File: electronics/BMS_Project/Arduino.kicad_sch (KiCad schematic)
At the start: 1 part

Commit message: Meeting 28.04.2023 worked on schematic
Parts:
- added JP1: SolderJumper_2_Open, symbol Jumper:SolderJumper_2_Open
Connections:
- net +5V: now also JP1.1 (A)
- net at XA1.AREF: now also JP1.2 (B)
- net switch_for_disconnecting_batteries renamed bat_main_switch
- no-connect marks 65 -> 64
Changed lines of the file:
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@@
   (no_connect (at 148.59 55.88))
   (no_connect (at 148.59 104.14))
-  (no_connect (at 82.55 114.3))
   (no_connect (at 82.55 40.64))
   (no_connect (at 148.59 45.72))
@@
     (stroke (width 0) (type default))
   )
+  (wire (pts (xy 66.04 114.3) (xy 69.85 114.3))
+    (stroke (width 0) (type default))
+  )
   (wire (pts (xy 72.39 137.16) (xy 82.55 137.16))
     (stroke (width 0) (type default))
@@
   )
   (wire (pts (xy 82.55 149.86) (xy 82.55 153.67))
+    (stroke (width 0) (type default))
+  )
+  (wire (pts (xy 77.47 114.3) (xy 82.55 114.3))
     (stroke (width 0) (type default))
   )
@@
     (effects (font (size 1.27 1.27)) (justify left))
   )
-  (hierarchical_label "switch_for_disconnecting_batteries" (shape bidirectional) (at 148.59 81.28 0) (fields_autoplaced)
+  (hierarchical_label "bat_main_switch" (shape bidirectional) (at 148.59 81.28 0) (fields_autoplaced)
     (effects (font (size 1.27 1.27)) (justify left))
   )
@@
     (effects (font (size 1.27 1.27)) (justify left))
   )
+  (symbol (lib_id "Jumper:SolderJumper_2_Open") (at 73.66 114.3 0) (unit 1)
+    (in_bom yes) (on_board yes) (dnp no)
+    (property "Reference" "JP1" (at 72.39 111.76 0)
+      (effects (font (size 1.27 1.27)))
+    )
+    (property "Value" "SolderJumper_2_Open" (at 64.77 118.11 0)
+      (effects (font (size 1.27 1.27)))
+    )
+    (property "Footprint" "" (at 73.66 114.3 0)
+      (effects (font (size 1.27 1.27)) hide)
+    )
+    (property "Datasheet" "~" (at 73.66 114.3 0)
+      (effects (font (size 1.27 1.27)) hide)
+    )
+    (pin "1")
+    (pin "2")
+    (instances
+      (project "BMS_Project"
+        (path "/524e7f14-feb0-4ca2-9425-a347c869bfa6/991268b7-e362-463f-9f04-bcec0fe70615"
+          (reference "JP1") (unit 1)
+        )
+      )
+    )
+  )
+  (symbol (lib_id "power:+5V") (at 66.04 114.3 0) (unit 1)
+    (in_bom yes) (on_board yes) (dnp no) (fields_autoplaced)
+    (property "Reference" "#PWR013" (at 66.04 118.11 0)
+      (effects (font (size 1.27 1.27)) hide)
+    )
+    (property "Value" "+5V" (at 66.04 110.49 0)
+      (effects (font (size 1.27 1.27)))
+    )
+    (property "Footprint" "" (at 66.04 114.3 0)
+      (effects (font (size 1.27 1.27)) hide)
+    )
+    (property "Datasheet" "" (at 66.04 114.3 0)
+      (effects (font (size 1.27 1.27)) hide)
+    )
+    (pin "1")
+    (instances
+      (project "BMS_Project"
+        (path "/524e7f14-feb0-4ca2-9425-a347c869bfa6/991268b7-e362-463f-9f04-bcec0fe70615"
+          (reference "#PWR013") (unit 1)
+        )
+      )
+    )
+  )
   (symbol (lib_id "power:+3.3V") (at 72.39 137.16 0) (unit 1)

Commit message: discord session with Johannes and Fabian, Schematic nearly done, all footprints fields filled
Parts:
- added SW1, SW3, SW4, SW5: SW_Push, Button_Switch_SMD:SW_Push_1P1T_NO_6x6mm_H9.5mm, symbol Switch:SW_Push
- JP1: footprint (none) -> Jumper:SolderJumper-2_P1.3mm_Open_Pad1.0x1.5mm
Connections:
- net +5V: now also SW1.2, SW3.2, SW4.2, SW5.2
- net Switch_0: now reaches XA1.D30
- net Switch_0: now also SW1.1
- net Switch_1: now reaches XA1.D31
- net Switch_1: now also SW3.1
- net Switch_2: now reaches XA1.D32
- net Switch_2: now also SW4.1
- net Switch_3: now reaches XA1.D33
- net Switch_3: now also SW5.1
- net Display_enable: now reaches XA1.D34
- no-connect marks 64 -> 59

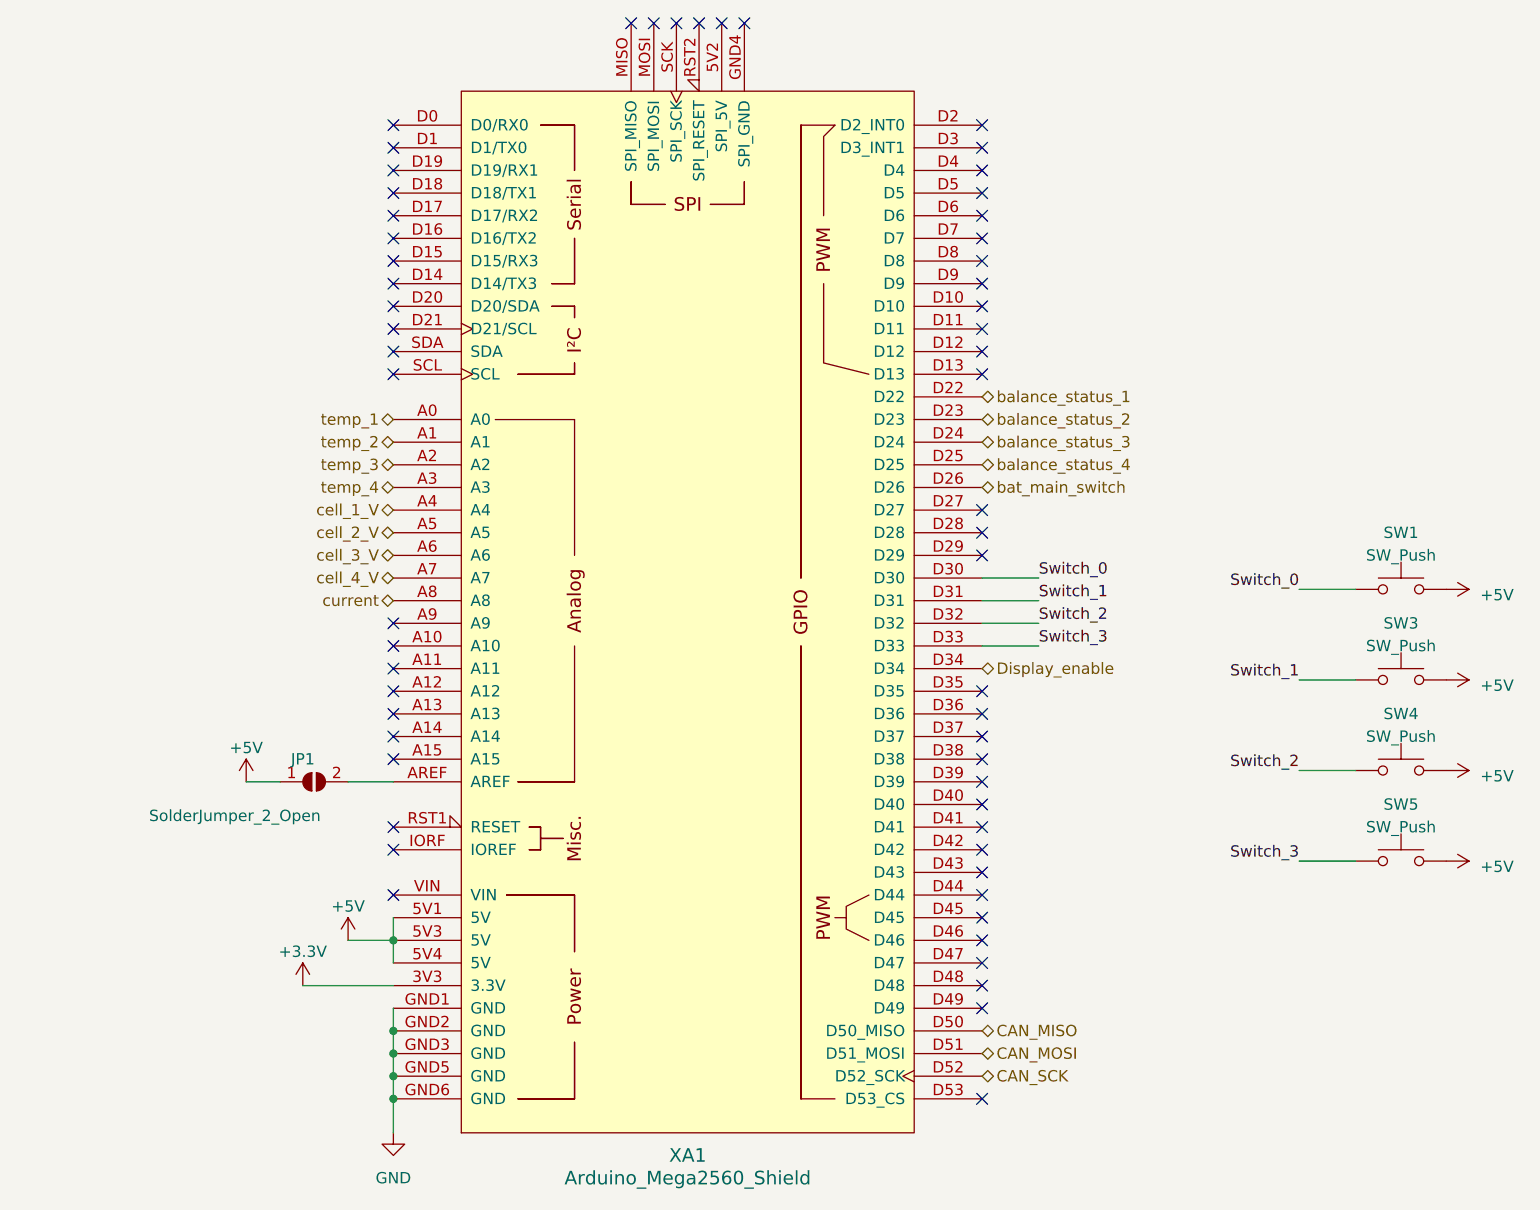
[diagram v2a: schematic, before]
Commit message: schematic done, starting with layout
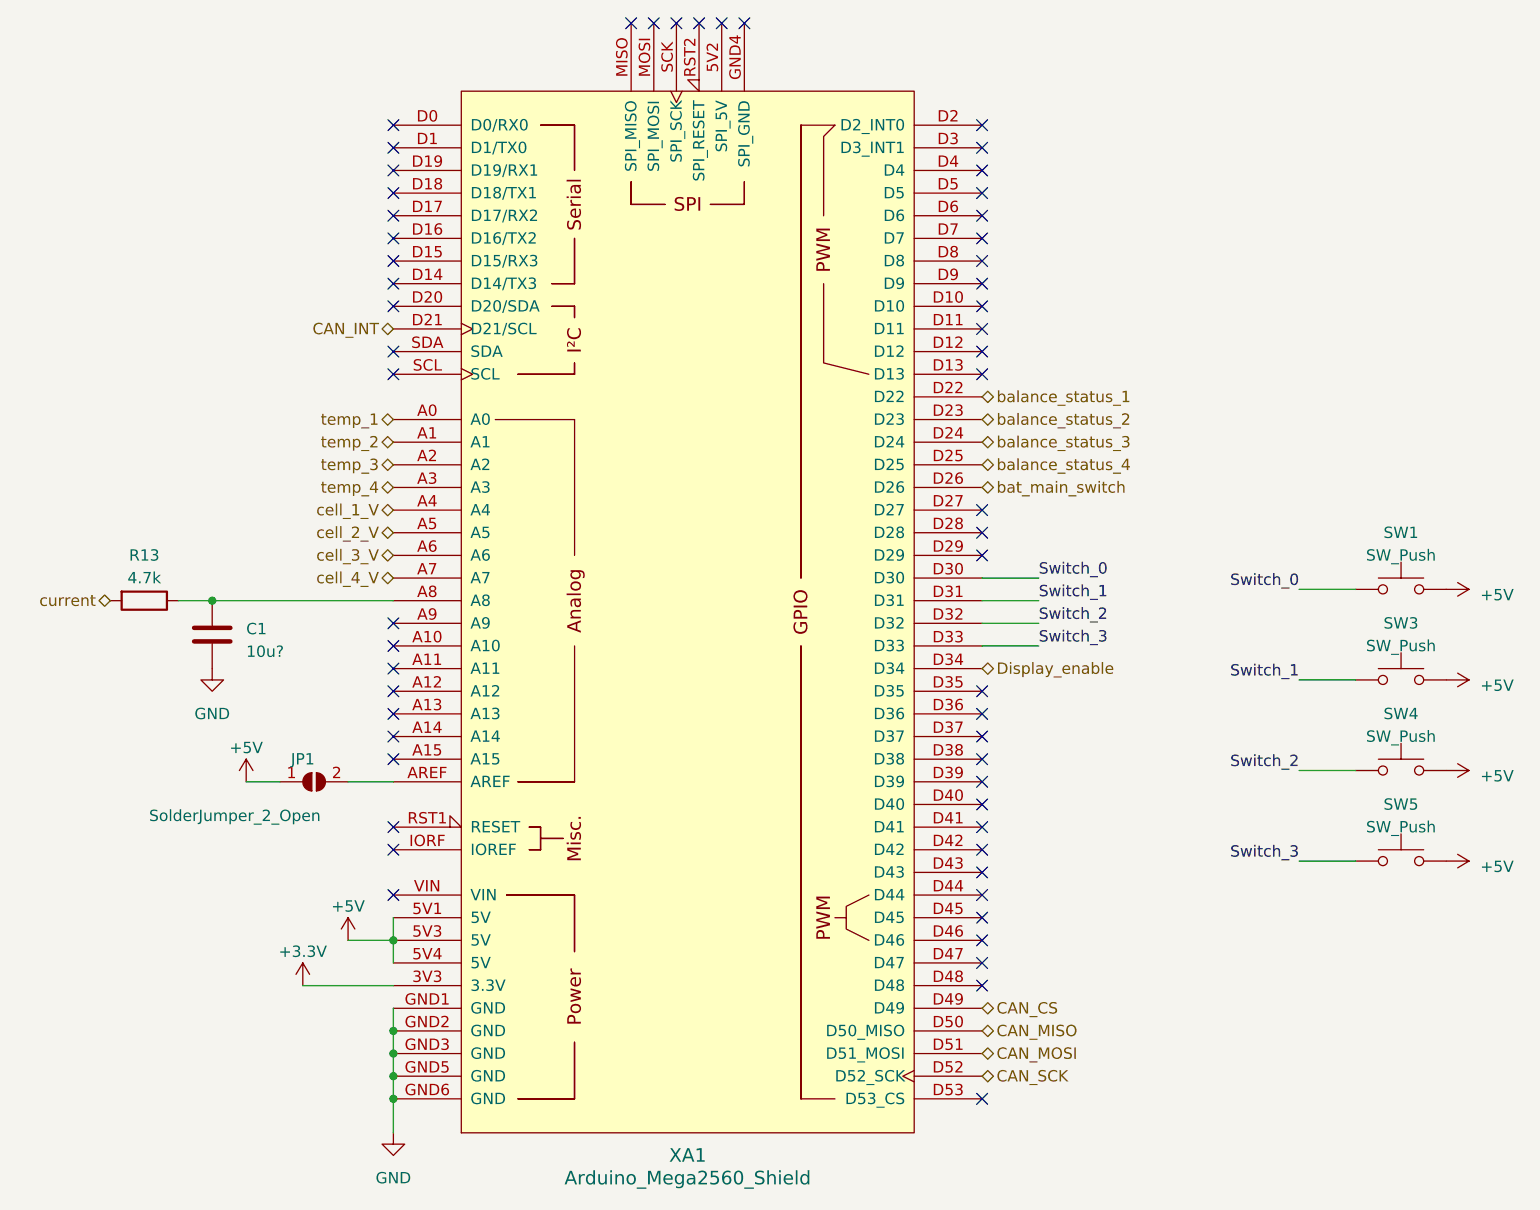
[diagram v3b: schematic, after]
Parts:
- added C1: 10u?, Capacitor_SMD:C_0805_2012Metric, symbol Device:C
- added R13: 4.7k, Resistor_THT:R_Axial_DIN0207_L6.3mm_D2.5mm_P10.16mm_Horizontal, symbol Device:R
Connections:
- net GND: now also C1.2
- net current: now also R13.2; no longer XA1.A8
- net CAN_INT: now reaches XA1.D21 (D21/SCL)
- net CAN_CS: now reaches XA1.D49
- new net: C1.1, R13.1, XA1.A8
- no-connect marks 59 -> 57
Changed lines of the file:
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@@
   (junction (at 82.55 144.78) (diameter 0) (color 0 0 0 0)
+  )
+  (junction (at 62.23 93.98) (diameter 0) (color 0 0 0 0)
   )
   (no_connect (at 82.55 96.52))
@@
   (no_connect (at 82.55 58.42))
   (no_connect (at 82.55 55.88))
-  (no_connect (at 148.59 139.7))
   (no_connect (at 148.59 116.84))
-  (no_connect (at 82.55 63.5))
   (no_connect (at 148.59 63.5))
   (no_connect (at 82.55 66.04))
@@
     (stroke (width 0) (type default))
   )
+  (wire (pts (xy 58.42 93.98) (xy 62.23 93.98))
+    (stroke (width 0) (type default))
+  )
   (wire (pts (xy 77.47 132.08) (xy 82.55 132.08))
     (stroke (width 0) (type default))
@@
   )
   (wire (pts (xy 82.55 144.78) (xy 82.55 147.32))
+    (stroke (width 0) (type default))
+  )
+  (wire (pts (xy 62.23 93.98) (xy 82.55 93.98))
     (stroke (width 0) (type default))
   )
@@
     (effects (font (size 1.27 1.27)) (justify left))
   )
-  (hierarchical_label "current" (shape bidirectional) (at 82.55 93.98 180) (fields_autoplaced)
+  (hierarchical_label "current" (shape bidirectional) (at 50.8 93.98 180) (fields_autoplaced)
     (effects (font (size 1.27 1.27)) (justify right))
   )
@@
     (effects (font (size 1.27 1.27)) (justify left))
   )
+  (hierarchical_label "CAN_CS" (shape bidirectional) (at 148.59 139.7 0) (fields_autoplaced)
+    (effects (font (size 1.27 1.27)) (justify left))
+  )
   (hierarchical_label "cell_1_V" (shape bidirectional) (at 82.55 83.82 180) (fields_autoplaced)
     (effects (font (size 1.27 1.27)) (justify right))
@@
   (hierarchical_label "balance_status_4" (shape bidirectional) (at 148.59 78.74 0) (fields_autoplaced)
     (effects (font (size 1.27 1.27)) (justify left))
+  )
+  (hierarchical_label "CAN_INT" (shape bidirectional) (at 82.55 63.5 180) (fields_autoplaced)
+    (effects (font (size 1.27 1.27)) (justify right))
   )
   (hierarchical_label "balance_status_3" (shape bidirectional) (at 148.59 76.2 0) (fields_autoplaced)
@@
     )
   )
+  (symbol (lib_id "Device:C") (at 62.23 97.79 0) (unit 1)
+    (in_bom yes) (on_board yes) (dnp no) (fields_autoplaced)
+    (property "Reference" "C1" (at 66.04 97.155 0)
+      (effects (font (size 1.27 1.27)) (justify left))
+    )
+    (property "Value" "10u?" (at 66.04 99.695 0)
+      (effects (font (size 1.27 1.27)) (justify left))
+    )
+    (property "Footprint" "Capacitor_SMD:C_0805_2012Metric" (at 63.1952 101.6 0)
+      (effects (font (size 1.27 1.27)) hide)
+    )
+    (property "Datasheet" "~" (at 62.23 97.79 0)
+      (effects (font (size 1.27 1.27)) hide)
+    )
+    (pin "1")
+    (pin "2")
+    (instances
+      (project "BMS_Project"
+        (path "/524e7f14-feb0-4ca2-9425-a347c869bfa6/991268b7-e362-463f-9f04-bcec0fe70615"
+          (reference "C1") (unit 1)
+        )
+      )
+      (project "Cell_holder_board"
+        (path "/c2697d40-f04f-4888-9ae9-ce0b7f222632/d1e5a9a1-ef5e-4043-b331-33dbe5a7732b"
+          (reference "C1") (unit 1)
+        )
+      )
+    )
+  )
   (symbol (lib_id "Switch:SW_Push") (at 195.58 92.71 0) (unit 1)
     (in_bom yes) (on_board yes) (dnp no) (fields_autoplaced)
@@
         (path "/524e7f14-feb0-4ca2-9425-a347c869bfa6/991268b7-e362-463f-9f04-bcec0fe70615"
           (reference "#PWR022") (unit 1)
+        )
+      )
+    )
+  )
+  (symbol (lib_id "power:GND") (at 62.23 101.6 0) (unit 1)
+    (in_bom yes) (on_board yes) (dnp no) (fields_autoplaced)
+    (property "Reference" "#PWR036" (at 62.23 107.95 0)
+      (effects (font (size 1.27 1.27)) hide)
+    )
+    (property "Value" "GND" (at 62.23 106.68 0)
+      (effects (font (size 1.27 1.27)))
+    )
+    (property "Footprint" "" (at 62.23 101.6 0)
+      (effects (font (size 1.27 1.27)) hide)
+    )
+    (property "Datasheet" "" (at 62.23 101.6 0)
+      (effects (font (size 1.27 1.27)) hide)
+    )
+    (pin "1")
+    (instances
+      (project "BMS_Project"
+        (path "/524e7f14-feb0-4ca2-9425-a347c869bfa6/991268b7-e362-463f-9f04-bcec0fe70615"
+          (reference "#PWR036") (unit 1)
         )
       )
@@
         )
       )
+    )
+  )
+  (symbol (lib_id "Device:R") (at 54.61 93.98 270) (unit 1)
+    (in_bom yes) (on_board yes) (dnp no) (fields_autoplaced)
+    (property "Reference" "R13" (at 54.61 88.9 90)
+      (effects (font (size 1.27 1.27)))
+    )
+    (property "Value" "4.7k" (at 54.61 91.44 90)
+      (effects (font (size 1.27 1.27)))
+    )
+    (property "Footprint" "Resistor_THT:R_Axial_DIN0207_L6.3mm_D2.5mm_P10.16mm_Horizontal" (at 54.61 92.202 90)
+      (effects (font (size 1.27 1.27)) hide)
+    )
+    (property "Datasheet" "~" (at 54.61 93.98 0)
+      (effects (font (size 1.27 1.27)) hide)
+    )
+    (pin "1")
+    (pin "2")
+    (instances
+      (project "BMS_Project"
+        (path "/524e7f14-feb0-4ca2-9425-a347c869bfa6/d8f12774-e346-4091-abf5-b4c43e81469c"
+          (reference "R13") (unit 1)
+        )
+        (path "/524e7f14-feb0-4ca2-9425-a347c869bfa6/991268b7-e362-463f-9f04-bcec0fe70615"
+          (reference "R17") (unit 1)
+        )
+      )
+      (project "Test_Projekt"
+        (path "/d5b120ca-a0f0-4b3f-8fab-ca010d94ac2e"
+          (reference "R9") (unit 1)
+        )
+      )
